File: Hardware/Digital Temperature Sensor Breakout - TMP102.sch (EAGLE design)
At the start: 17 parts, among them U1 TMP1021:1

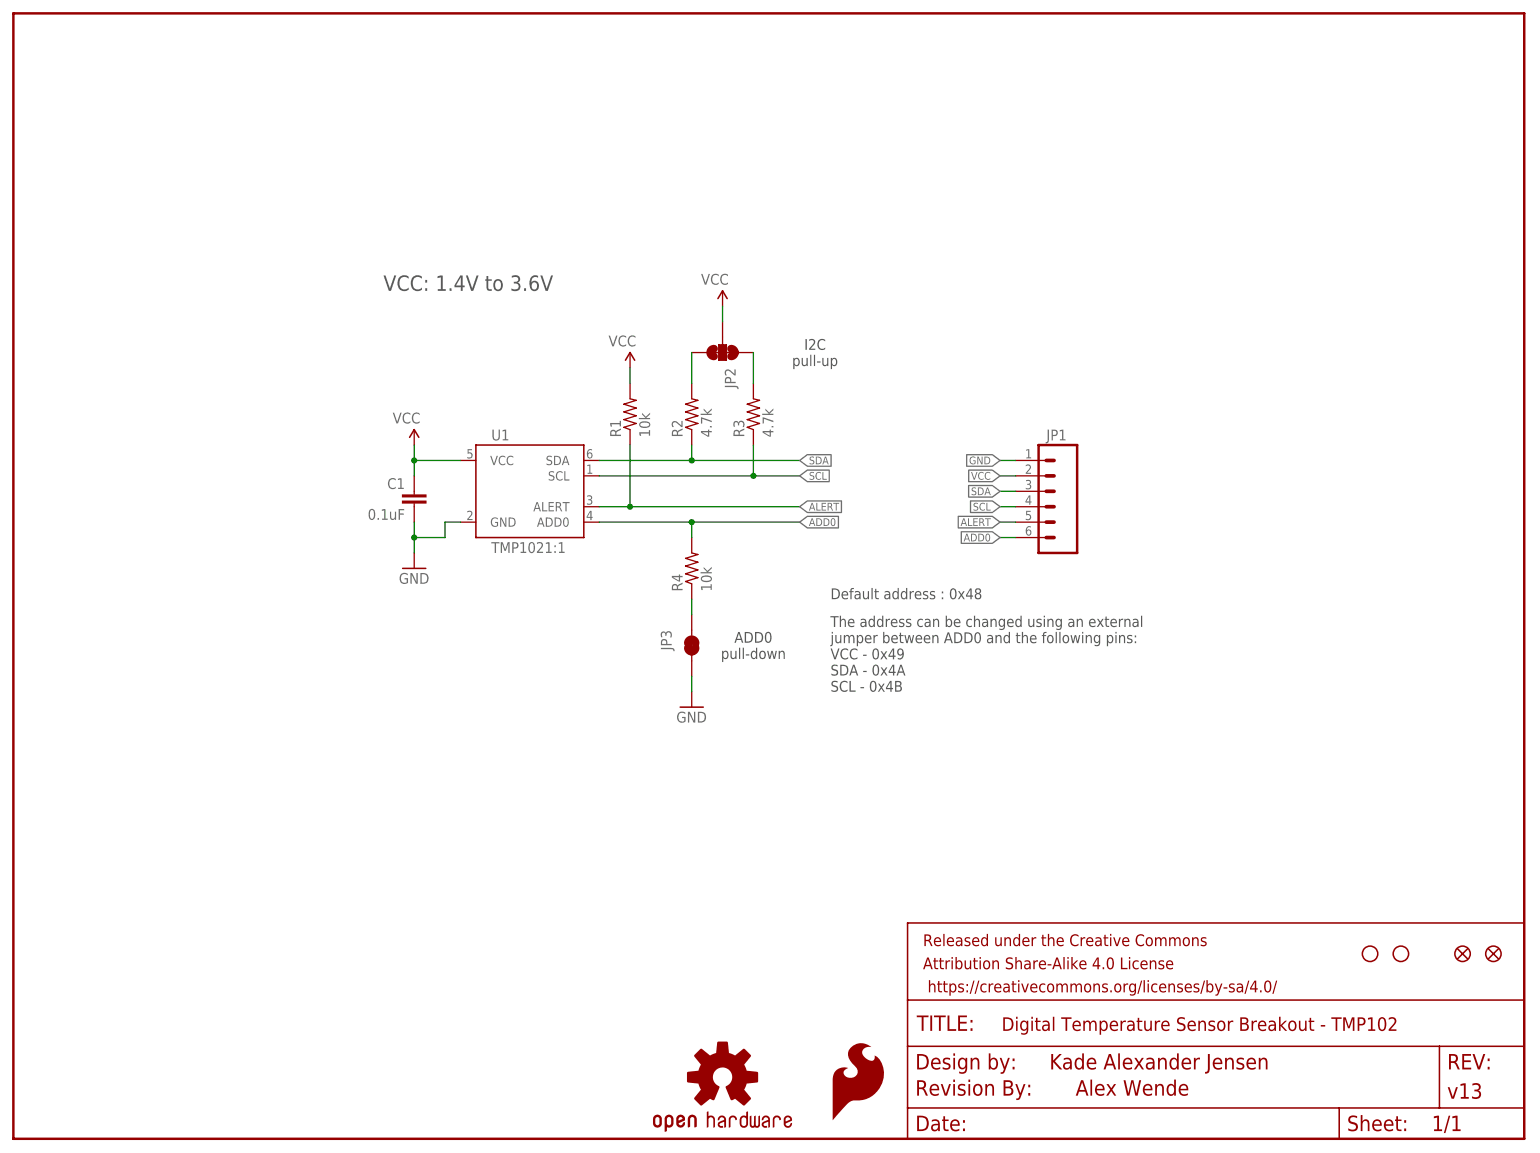
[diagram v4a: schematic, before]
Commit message: QC Fixes
Updated parts with PROD_ID attributes
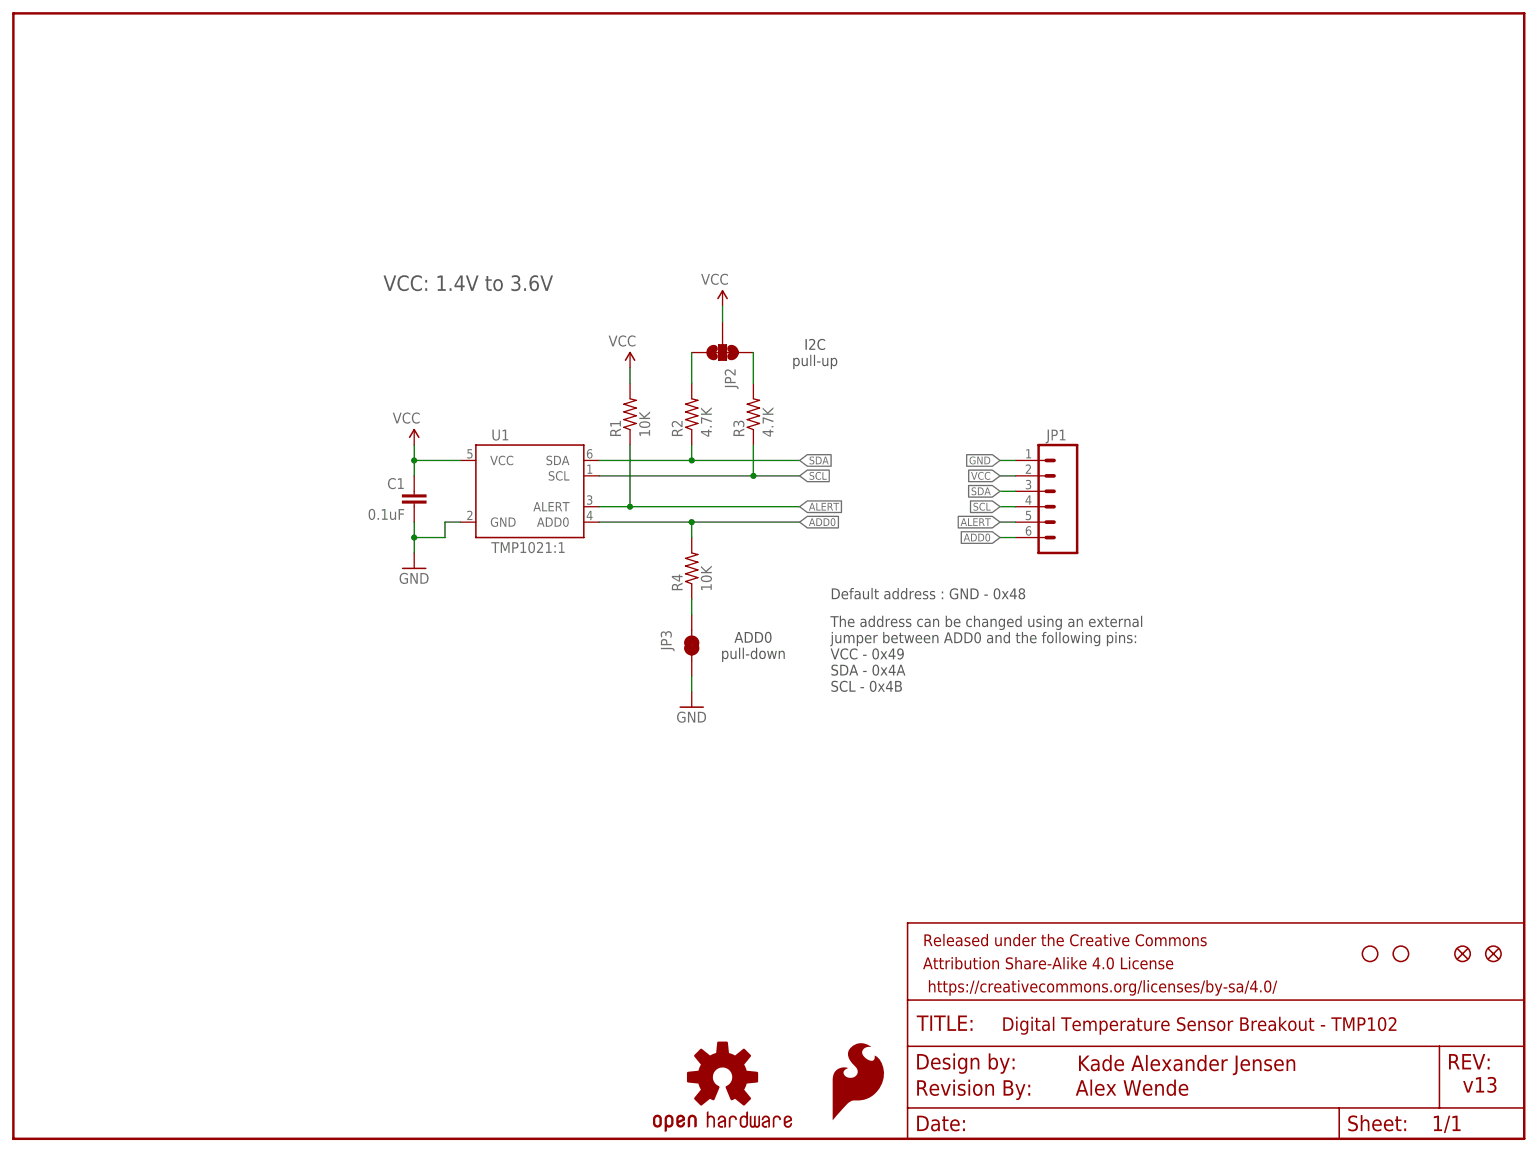
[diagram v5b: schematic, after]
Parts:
- C1: device SparkFun:CAP0603-CAP -> SparkFun-Capacitors:0.1UF-25V(+80/-20%)(0603)
- FRAME2: value (none) -> FRAME-LETTER; DESIGNER Kade Alexander Jensen -> (none); VERSION v13 -> (none)
- R1, R4: value 10k -> 10K; device SparkFun:RESISTOR0603-RES -> SparkFun-Resistors:10KOHM-1/10W-1%(0603)0603
- R2, R3: value 4.7k -> 4.7K; device SparkFun:RESISTOR0603-RES -> SparkFun-Resistors:4.7KOHM-1/10W-1%(0603)
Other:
- note added: "Default address : GND - 0x48"
- note added: "Kade Alexander Jensen"
- note added: "v13"
- note removed: "Default address : 0x48"
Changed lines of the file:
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@@
 <setting verticaltext="up"/>
 </settings>
-<grid distance="0.1" unitdist="inch" unit="inch" style="lines" multiple="1" display="yes" altdistance="0.01" altunitdist="inch" altunit="inch"/>
+<grid distance="0.1" unitdist="inch" unit="inch" style="lines" multiple="1" display="no" altdistance="0.01" altunitdist="inch" altunit="inch"/>
 <layers>
 <layer number="1" name="Top" color="4" fill="1" visible="no" active="no"/>
@@
 </classes>
 <parts>
-<part name="R2" library="SparkFun" deviceset="RESISTOR" device="0603-RES" value="4.7k"/>
-<part name="R3" library="SparkFun" deviceset="RESISTOR" device="0603-RES" value="4.7k"/>
-<part name="R1" library="SparkFun" deviceset="RESISTOR" device="0603-RES" value="10k"/>
-<part name="C1" library="SparkFun" deviceset="CAP" device="0603-CAP" value="0.1uF"/>
+<part name="R2" library="SparkFun-Resistors" deviceset="4.7KOHM-1/10W-1%(0603)" device="" value="4.7K"/>
+<part name="R3" library="SparkFun-Resistors" deviceset="4.7KOHM-1/10W-1%(0603)" device="" value="4.7K"/>
+<part name="R1" library="SparkFun-Resistors" deviceset="10KOHM-1/10W-1%(0603)" device="0603" value="10K"/>
+<part name="C1" library="SparkFun-Capacitors" deviceset="0.1UF-25V(+80/-20%)(0603)" device="" value="0.1uF"/>
 <part name="JP5" library="SparkFun" deviceset="FIDUCIAL" device="1X2"/>
 <part name="JP6" library="SparkFun" deviceset="FIDUCIAL" device="1X2"/>
@@
 <part name="JP7" library="SparkFun" deviceset="STAND-OFF" device="TIGHT"/>
 <part name="JP8" library="SparkFun" deviceset="STAND-OFF" device="TIGHT"/>
-<part name="FRAME2" library="SparkFun-Aesthetics" deviceset="FRAME-LETTER" device="">
-<attribute name="DESIGNER" value="Kade Alexander Jensen"/>
-<attribute name="VERSION" value="v13"/>
-</part>
+<part name="FRAME2" library="SparkFun-Aesthetics" deviceset="FRAME-LETTER" device=""/>
 <part name="SUPPLY1" library="SparkFun-Aesthetics" deviceset="VCC" device=""/>
 <part name="GND1" library="SparkFun" deviceset="GND" device=""/>
@@
 <part name="LOGO2" library="SparkFun-Aesthetics" deviceset="SFE_LOGO_FLAME" device=".1_INCH"/>
 <part name="LOGO3" library="SparkFun-Aesthetics" deviceset="OSHW-LOGO" device="S"/>
-<part name="R4" library="SparkFun" deviceset="RESISTOR" device="0603-RES" value="10k"/>
+<part name="R4" library="SparkFun-Resistors" deviceset="10KOHM-1/10W-1%(0603)" device="0603" value="10K"/>
 </parts>
 <sheets>
@@
 <text x="132.08" y="129.54" size="1.778" layer="97" align="center">I2C
 pull-up</text>
-<text x="134.62" y="88.9" size="1.778" layer="97">Default address : 0x48</text>
+<text x="134.62" y="88.9" size="1.778" layer="97">Default address : GND - 0x48</text>
 <text x="134.62" y="73.66" size="1.778" layer="97">The address can be changed using an external
 jumper between ADD0 and the following pins:
@@
 SDA - 0x4A
 SCL - 0x4B</text>
+<text x="175.26" y="11.176" size="2.54" layer="94">Kade Alexander Jensen</text>
+<text x="238.76" y="7.62" size="2.54" layer="94">v13</text>
 </plain>
 <instances>
@@
 <attribute name="SHEET" x="233.68" y="1.27" size="2.54" layer="94" font="vector"/>
 <attribute name="DRAWING_NAME" x="162.814" y="17.78" size="2.2352" layer="94" font="vector"/>
-<attribute name="DESIGNER" x="170.688" y="11.43" size="2.54" layer="94"/>
-<attribute name="VERSION" x="236.22" y="6.604" size="2.54" layer="94" font="vector"/>
 </instance>
 <instance part="SUPPLY1" gate="G$1" x="66.04" y="114.3" rot="MR0"/>
